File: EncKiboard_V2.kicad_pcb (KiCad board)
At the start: 2 copper layers, 94 x 94 mm, 48 parts, among them IC1 4094D, IC2 4094D, M3 MountingHole_3.2mm_M3, SW1 Rotary_Encoder_Switch, U0 ProMicro, U1 CherryMX_LED, U10 CherryMX_LED, U11 CherryMX_LED, U12 CherryMX_LED, U2 CherryMX_LED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

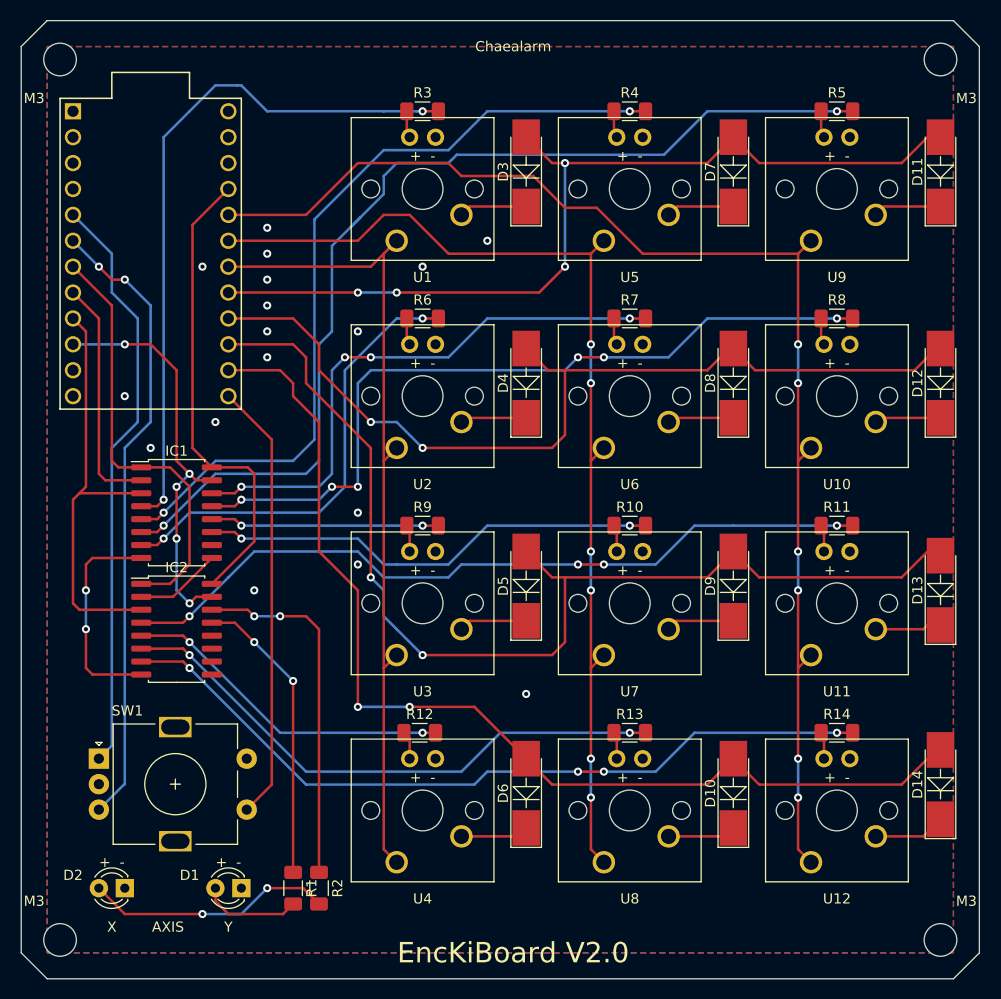
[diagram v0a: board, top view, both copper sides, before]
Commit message: Edit wrong diode position
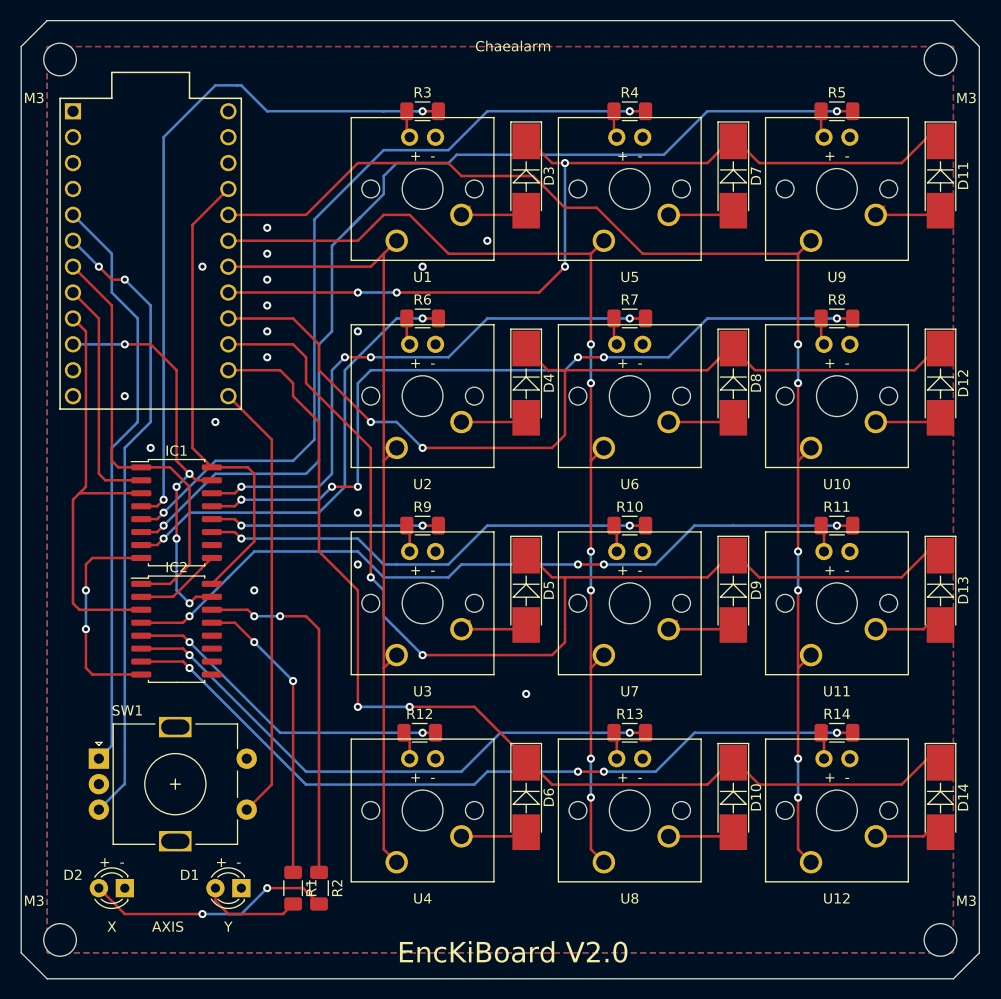
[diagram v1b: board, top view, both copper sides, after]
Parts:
- D10, D11, D12, D13, D14, D3, D4, D5, D6, D7, D8, D9: value DIODE -> 1N4148_SMD
- moved D14 1.27 mm to (196.8, 137.2), turned to 270 degrees
- moved D10 0.41 mm to (176.5, 137.2), turned to 270 degrees
- moved D11 0.41 mm to (196.8, 76.2), turned to 270 degrees
- moved D3 0.41 mm to (156.2, 76.2), turned to 270 degrees
- moved D5 0.41 mm to (156.2, 116.8), turned to 270 degrees
- moved D6 0.41 mm to (156.2, 137.2), turned to 270 degrees
- moved D7 0.41 mm to (176.5, 76.2), turned to 270 degrees
- moved D9 0.41 mm to (176.5, 116.8), turned to 270 degrees
- turned D12 to 270 degrees
- turned D13 to 270 degrees
- turned D4 to 270 degrees
- turned D8 to 270 degrees
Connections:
- D14 pad 1: Net-(D14-Pad1) -> Net-(D10-Pad1)
- D14 pad 2: Net-(D10-Pad2) -> Net-(D14-Pad2)
- D3 pad 1: Net-(D3-Pad1) -> Net-(D11-Pad1)
- D3 pad 2: Net-(D11-Pad2) -> Net-(D3-Pad2)
- D4 pad 1: Net-(D4-Pad1) -> Net-(D12-Pad1)
- D4 pad 2: Net-(D12-Pad2) -> Net-(D4-Pad2)
- D5 pad 1: Net-(D5-Pad1) -> Net-(D13-Pad1)
- D5 pad 2: Net-(D13-Pad2) -> Net-(D5-Pad2)
- D6 pad 1: Net-(D6-Pad1) -> Net-(D10-Pad1)
- D6 pad 2: Net-(D10-Pad2) -> Net-(D6-Pad2)
- D7 pad 1: Net-(D7-Pad1) -> Net-(D11-Pad1)
- D7 pad 2: Net-(D11-Pad2) -> Net-(D7-Pad2)
- D8 pad 1: Net-(D8-Pad1) -> Net-(D12-Pad1)
- D8 pad 2: Net-(D12-Pad2) -> Net-(D8-Pad2)
- D9 pad 1: Net-(D9-Pad1) -> Net-(D13-Pad1)
- D9 pad 2: Net-(D13-Pad2) -> Net-(D9-Pad2)
- U0 pad 14: Net-(D10-Pad2) -> Net-(D10-Pad1)
- U0 pad 15: Net-(D13-Pad2) -> Net-(D13-Pad1)
- U0 pad 16: Net-(D12-Pad2) -> Net-(D12-Pad1)
- U0 pad 17: Net-(D11-Pad2) -> Net-(D11-Pad1)
- U1 pad 1: Net-(D3-Pad1) -> Net-(D3-Pad2)
- U10 pad 1: Net-(D12-Pad1) -> Net-(D12-Pad2)
- U11 pad 1: Net-(D13-Pad1) -> Net-(D13-Pad2)
- U12 pad 1: Net-(D14-Pad1) -> Net-(D14-Pad2)
- U2 pad 1: Net-(D4-Pad1) -> Net-(D4-Pad2)
- U3 pad 1: Net-(D5-Pad1) -> Net-(D5-Pad2)
- U4 pad 1: Net-(D6-Pad1) -> Net-(D6-Pad2)
- U5 pad 1: Net-(D7-Pad1) -> Net-(D7-Pad2)
- U6 pad 1: Net-(D8-Pad1) -> Net-(D8-Pad2)
- U7 pad 1: Net-(D9-Pad1) -> Net-(D9-Pad2)
- U8 pad 1: Net-(D10-Pad1) -> Net-(D10-Pad2)
- U9 pad 1: Net-(D11-Pad1) -> Net-(D11-Pad2)
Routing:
- net Net-(D13-Pad2): track 108.1 -> 7.05 mm, vias 2 -> 0
- net Net-(D13-Pad1): track 7.05 -> 108.1 mm, vias 0 -> 2
- net Net-(D10-Pad2): track 105.1 -> 6.69 mm, vias 2 -> 0
- net Net-(D10-Pad1): track 6.69 -> 105.1 mm, vias 0 -> 2
- net Net-(D12-Pad2): track 90.8 -> 6.52 mm, vias 2 -> 0
- net Net-(D12-Pad1): track 6.52 -> 90.8 mm, vias 0 -> 2
- net Net-(D11-Pad2): track 89.1 -> 6.69 mm, vias 4 -> 0
- net Net-(D11-Pad1): track 6.69 -> 89.1 mm, vias 0 -> 4
- net Net-(D14-Pad2): track 0.00 -> 7.05 mm
- net Net-(D14-Pad1): track 7.05 -> 0.00 mm
- net Net-(D9-Pad2): track 0.00 -> 6.69 mm
- net Net-(D9-Pad1): track 6.69 -> 0.00 mm
- net Net-(D7-Pad1): track 6.69 -> 0.00 mm
- net Net-(D5-Pad2): track 0.00 -> 6.69 mm
- net Net-(D5-Pad1): track 6.69 -> 0.00 mm
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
